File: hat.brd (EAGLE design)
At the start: 56 x 65 mm, 13 parts, among them J1 RASPBERRYPI-40-PIN-GPIO_PTH_N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

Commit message: tweaks
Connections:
- net N$1 renamed 3.3VGP10
- net N$10 renamed 5VGP18
- net N$14 renamed GP10
- net N$15 renamed GP21
- net N$18 renamed GP12
- net N$19 renamed GP18
- net N$2 renamed 3.3VGP12
- net N$3 renamed 3.3VGP18
- net N$4 renamed 3.3VGP21
- net N$7 renamed 5VGP10
- net N$8 renamed 5VGP12
- net N$9 renamed 5VGP21
- removed net N$12: C1.+, DC5VIN.1, DC5VOUT.1, INT_5V_JMPR.2, J3.2
- removed net N$13: J1.9, J2.1, J3.1
- removed net N$17: C1.-, DC5VIN.2, DC5VOUT.2, J1.6
- removed net N$5: J1.1, J2.2
- removed net N$6: INT_5V_JMPR.1, J1.2
- net 3.3V: now also J1.1, J2.2
- net 5V: now also C1.+, DC5VIN.1, DC5VOUT.1, INT_5V_JMPR.1, INT_5V_JMPR.2, J1.2, J3.2
- net GND: now also C1.-, DC5VIN.2, DC5VOUT.2, J1.6, J1.9, J2.1, J3.1
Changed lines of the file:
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@@
 <drawing>
 <settings>
-<setting alwaysvectorfont="no"/>
+<setting alwaysvectorfont="yes"/>
 <setting verticaltext="up"/>
 </settings>
@@
 <contactref element="J1" pad="34"/>
 <contactref element="J1" pad="39"/>
-<wire x1="3.81" y1="48.26" x2="6.35" y2="55.88" width="0" layer="19" extent="1-1"/>
-<wire x1="3.81" y1="43.18" x2="3.81" y2="48.26" width="0" layer="19" extent="1-1"/>
-<wire x1="6.35" y1="38.1" x2="3.81" y2="43.18" width="0" layer="19" extent="1-1"/>
-<wire x1="3.81" y1="30.48" x2="6.35" y2="38.1" width="0" layer="19" extent="1-1"/>
-<wire x1="3.81" y1="22.86" x2="3.81" y2="30.48" width="0" layer="19" extent="1-1"/>
-</signal>
-<signal name="3.3V">
-<contactref element="J1" pad="17"/>
-</signal>
-<signal name="5V">
-<contactref element="J1" pad="4"/>
-</signal>
-<signal name="N$1">
-<contactref element="J1" pad="19"/>
-<contactref element="J2" pad="6"/>
-<wire x1="13.97" y1="53.34" x2="6.35" y2="30.48" width="0" layer="19" extent="1-1"/>
-</signal>
-<signal name="N$2">
-<contactref element="J1" pad="32"/>
-<contactref element="J2" pad="5"/>
-<wire x1="13.97" y1="50.8" x2="3.81" y2="45.72" width="0" layer="19" extent="1-1"/>
-</signal>
-<signal name="N$3">
-<contactref element="J1" pad="40"/>
-<contactref element="J2" pad="3"/>
-<wire x1="13.97" y1="45.72" x2="3.81" y2="55.88" width="0" layer="19" extent="1-1"/>
-</signal>
-<signal name="N$4">
-<contactref element="J1" pad="12"/>
-<contactref element="J2" pad="4"/>
-<wire x1="13.97" y1="48.26" x2="3.81" y2="20.32" width="0" layer="19" extent="1-1"/>
-</signal>
-<signal name="N$5">
-<contactref element="J1" pad="1"/>
-<contactref element="J2" pad="2"/>
-<wire x1="6.35" y1="7.62" x2="13.97" y2="43.18" width="0" layer="19" extent="1-1"/>
-</signal>
-<signal name="N$6">
-<contactref element="J1" pad="2"/>
-<contactref element="INT_5V_JMPR" pad="1"/>
-<wire x1="11.85" y1="7.62" x2="3.81" y2="7.62" width="0" layer="19" extent="1-1"/>
-</signal>
-<signal name="N$7">
-<contactref element="J3" pad="6"/>
-<contactref element="R1" pad="1"/>
-<wire x1="24.13" y1="53.34" x2="28.36" y2="55.88" width="0" layer="19" extent="1-1"/>
-</signal>
-<signal name="N$8">
-<contactref element="J3" pad="5"/>
-<contactref element="R2" pad="1"/>
-<wire x1="24.13" y1="50.8" x2="28.36" y2="50.8" width="0" layer="19" extent="1-1"/>
-</signal>
-<signal name="N$9">
-<contactref element="J3" pad="3"/>
-<contactref element="R4" pad="1"/>
-<wire x1="24.13" y1="45.72" x2="28.36" y2="40.64" width="0" layer="19" extent="1-1"/>
-</signal>
-<signal name="N$10">
-<contactref element="J3" pad="4"/>
-<contactref element="R3" pad="1"/>
-<wire x1="24.13" y1="48.26" x2="28.36" y2="45.72" width="0" layer="19" extent="1-1"/>
-</signal>
-<signal name="N$15">
-<contactref element="R4" pad="2"/>
-<contactref element="GPIO1821" pad="2"/>
-<wire x1="52.07" y1="40.64" x2="30.06" y2="40.64" width="0" layer="19" extent="1-1"/>
-</signal>
-<signal name="N$17">
+<contactref element="J1" pad="9"/>
 <contactref element="J1" pad="6"/>
 <contactref element="DC5VIN" pad="2"/>
 <contactref element="DC5VOUT" pad="2"/>
 <contactref element="C1" pad="-"/>
-<wire x1="3.81" y1="12.7" x2="15.24" y2="16.47" width="0" layer="19" extent="1-1"/>
-<wire x1="27.94" y1="3.81" x2="3.81" y2="12.7" width="0" layer="19" extent="1-1"/>
+<contactref element="J2" pad="1"/>
+<contactref element="J3" pad="1"/>
+<wire x1="13.97" y1="40.64" x2="24.13" y2="40.64" width="0" layer="19" extent="1-1"/>
+<wire x1="6.35" y1="38.1" x2="13.97" y2="40.64" width="0" layer="19" extent="1-1"/>
+<wire x1="3.81" y1="43.18" x2="6.35" y2="38.1" width="0" layer="19" extent="1-1"/>
+<wire x1="3.81" y1="48.26" x2="3.81" y2="43.18" width="0" layer="19" extent="1-1"/>
+<wire x1="6.35" y1="55.88" x2="3.81" y2="48.26" width="0" layer="19" extent="1-1"/>
+<wire x1="3.81" y1="30.48" x2="6.35" y2="38.1" width="0" layer="19" extent="1-1"/>
+<wire x1="3.81" y1="22.86" x2="3.81" y2="30.48" width="0" layer="19" extent="1-1"/>
+<wire x1="6.35" y1="17.78" x2="3.81" y2="22.86" width="0" layer="19" extent="1-1"/>
+<wire x1="3.81" y1="12.7" x2="6.35" y2="17.78" width="0" layer="19" extent="1-1"/>
+<wire x1="15.24" y1="16.47" x2="6.35" y2="17.78" width="0" layer="19" extent="1-1"/>
+<wire x1="27.94" y1="3.81" x2="15.24" y2="16.47" width="0" layer="19" extent="1-1"/>
 <wire x1="39.37" y1="3.81" x2="27.94" y2="3.81" width="0" layer="19" extent="1-1"/>
 </signal>
-<signal name="N$12">
+<signal name="3.3V">
+<contactref element="J1" pad="17"/>
+<contactref element="J1" pad="1"/>
+<contactref element="J2" pad="2"/>
+<wire x1="6.35" y1="27.94" x2="13.97" y2="43.18" width="0" layer="19" extent="1-1"/>
+<wire x1="6.35" y1="7.62" x2="6.35" y2="27.94" width="0" layer="19" extent="1-1"/>
+</signal>
+<signal name="5V">
+<contactref element="J1" pad="4"/>
+<contactref element="J1" pad="2"/>
+<contactref element="INT_5V_JMPR" pad="1"/>
 <contactref element="DC5VIN" pad="1"/>
 <contactref element="DC5VOUT" pad="1"/>
@@
 <contactref element="J3" pad="2"/>
 <contactref element="INT_5V_JMPR" pad="2"/>
+<wire x1="15.24" y1="11.47" x2="24.13" y2="43.18" width="0" layer="19" extent="1-1"/>
 <wire x1="13.55" y1="7.62" x2="15.24" y2="11.47" width="0" layer="19" extent="1-1"/>
+<wire x1="11.85" y1="7.62" x2="13.55" y2="7.62" width="0" layer="19" extent="1-1"/>
+<wire x1="3.81" y1="7.62" x2="11.85" y2="7.62" width="0" layer="19" extent="1-1"/>
+<wire x1="3.81" y1="10.16" x2="3.81" y2="7.62" width="0" layer="19" extent="1-1"/>
 <wire x1="22.86" y1="3.81" x2="13.55" y2="7.62" width="0" layer="19" extent="1-1"/>
 <wire x1="34.29" y1="3.81" x2="22.86" y2="3.81" width="0" layer="19" extent="1-1"/>
-<wire x1="24.13" y1="43.18" x2="13.55" y2="7.62" width="0" layer="19" extent="1-1"/>
-</signal>
-<signal name="N$13">
-<contactref element="J1" pad="9"/>
-<contactref element="J2" pad="1"/>
-<contactref element="J3" pad="1"/>
-<wire x1="13.97" y1="40.64" x2="6.35" y2="17.78" width="0" layer="19" extent="1-1"/>
-<wire x1="24.13" y1="40.64" x2="13.97" y2="40.64" width="0" layer="19" extent="1-1"/>
-</signal>
-<signal name="N$14">
+</signal>
+<signal name="3.3VGP10">
+<contactref element="J1" pad="19"/>
+<contactref element="J2" pad="6"/>
+<wire x1="6.35" y1="30.48" x2="13.97" y2="53.34" width="0" layer="19" extent="1-1"/>
+</signal>
+<signal name="3.3VGP12">
+<contactref element="J1" pad="32"/>
+<contactref element="J2" pad="5"/>
+<wire x1="3.81" y1="45.72" x2="13.97" y2="50.8" width="0" layer="19" extent="1-1"/>
+</signal>
+<signal name="3.3VGP18">
+<contactref element="J1" pad="40"/>
+<contactref element="J2" pad="3"/>
+<wire x1="13.97" y1="45.72" x2="3.81" y2="55.88" width="0" layer="19" extent="1-1"/>
+</signal>
+<signal name="3.3VGP21">
+<contactref element="J1" pad="12"/>
+<contactref element="J2" pad="4"/>
+<wire x1="3.81" y1="20.32" x2="13.97" y2="48.26" width="0" layer="19" extent="1-1"/>
+</signal>
+<signal name="5VGP10">
+<contactref element="J3" pad="6"/>
+<contactref element="R1" pad="1"/>
+<wire x1="24.13" y1="53.34" x2="28.36" y2="55.88" width="0" layer="19" extent="1-1"/>
+</signal>
+<signal name="5VGP12">
+<contactref element="J3" pad="5"/>
+<contactref element="R2" pad="1"/>
+<wire x1="24.13" y1="50.8" x2="28.36" y2="50.8" width="0" layer="19" extent="1-1"/>
+</signal>
+<signal name="5VGP21">
+<contactref element="J3" pad="3"/>
+<contactref element="R4" pad="1"/>
+<wire x1="28.36" y1="40.64" x2="24.13" y2="45.72" width="0" layer="19" extent="1-1"/>
+</signal>
+<signal name="5VGP18">
+<contactref element="J3" pad="4"/>
+<contactref element="R3" pad="1"/>
+<wire x1="24.13" y1="48.26" x2="28.36" y2="45.72" width="0" layer="19" extent="1-1"/>
+</signal>
+<signal name="GP21">
+<contactref element="R4" pad="2"/>
+<contactref element="GPIO1821" pad="2"/>
+<wire x1="30.06" y1="40.64" x2="52.07" y2="40.64" width="0" layer="19" extent="1-1"/>
+</signal>
+<signal name="GP10">
 <contactref element="R1" pad="2"/>
 <contactref element="GPIO1012" pad="1"/>
-<wire x1="52.07" y1="55.88" x2="30.06" y2="55.88" width="0" layer="19" extent="1-1"/>
-</signal>
-<signal name="N$18">
+<wire x1="30.06" y1="55.88" x2="52.07" y2="55.88" width="0" layer="19" extent="1-1"/>
+</signal>
+<signal name="GP12">
 <contactref element="R2" pad="2"/>
 <contactref element="GPIO1012" pad="2"/>
-<wire x1="52.07" y1="50.8" x2="30.06" y2="50.8" width="0" layer="19" extent="1-1"/>
-</signal>
-<signal name="N$19">
+<wire x1="30.06" y1="50.8" x2="52.07" y2="50.8" width="0" layer="19" extent="1-1"/>
+</signal>
+<signal name="GP18">
 <contactref element="R3" pad="2"/>
 <contactref element="GPIO1821" pad="1"/>
-<wire x1="52.07" y1="45.72" x2="30.06" y2="45.72" width="0" layer="19" extent="1-1"/>
+<wire x1="30.06" y1="45.72" x2="52.07" y2="45.72" width="0" layer="19" extent="1-1"/>
 </signal>
 </signals>

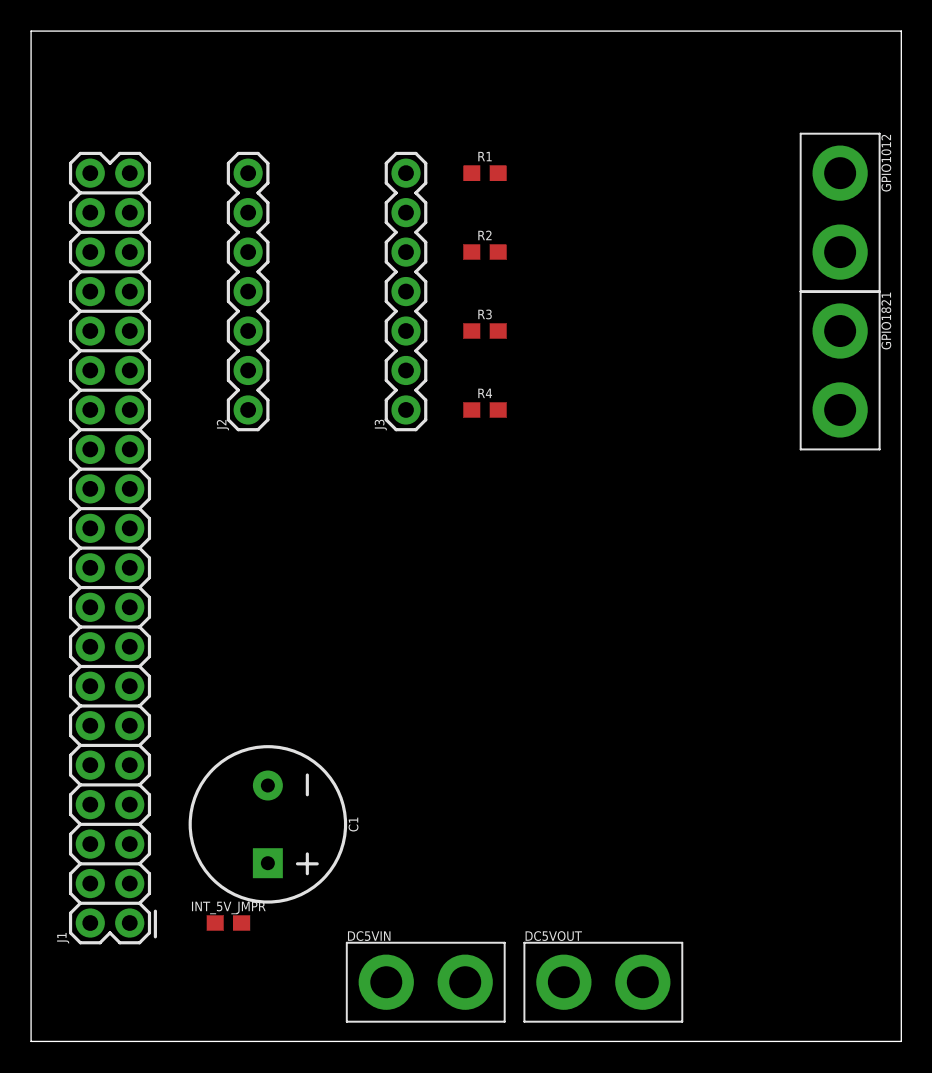
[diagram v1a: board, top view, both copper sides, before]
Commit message: shrunk board, double sided
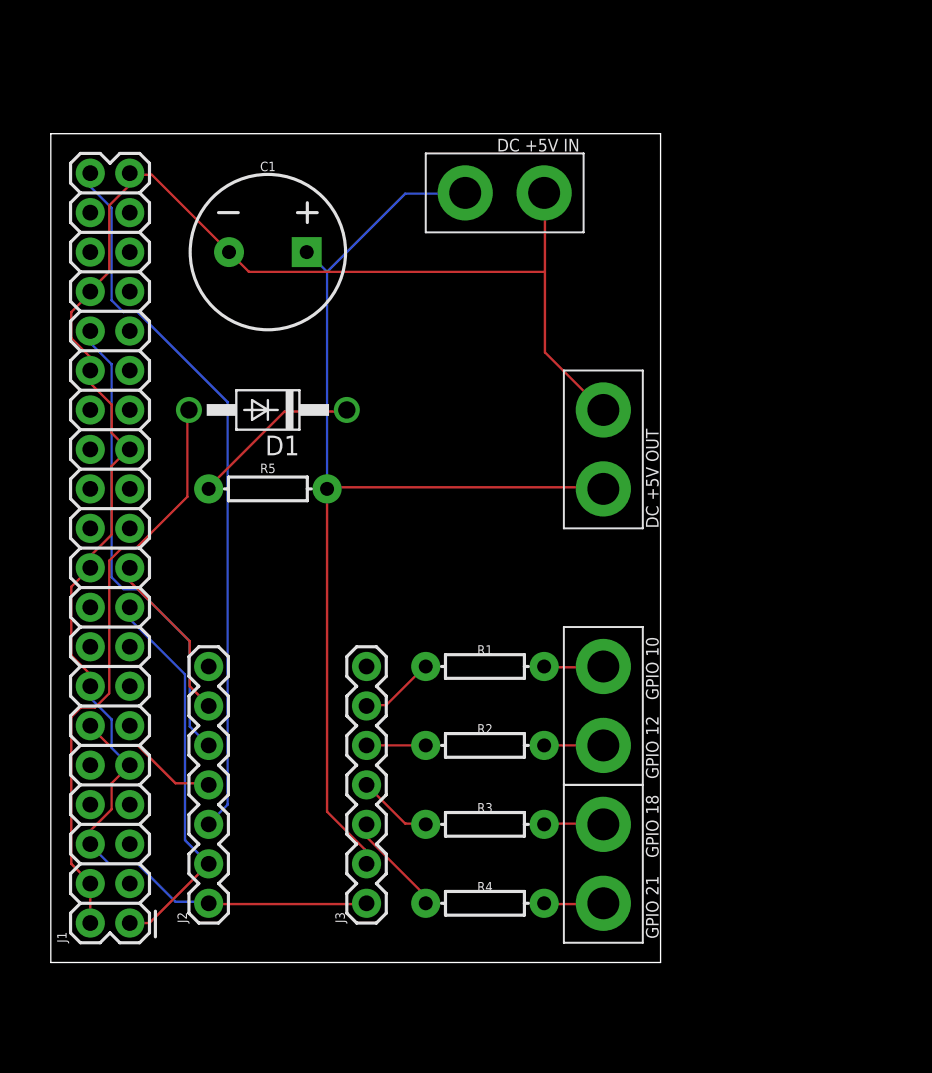
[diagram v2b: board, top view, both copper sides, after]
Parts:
- removed INT_5V_JMPR: 0, SparkFun-Resistors:0603
- added D1: 1N4004, diode:DO41-10
- added R5: (no value), SparkFun-Resistors:AXIAL-0.3
- R1, R2, R3, R4: value 470 -> (none); device SparkFun-Resistors:0603 -> SparkFun-Resistors:AXIAL-0.3
- moved DC5VIN 51.1 mm to (30.5, 54.6)
- moved C1 36.8 mm to (15.2, 50.8), turned to 0 degrees
- moved GPIO1012 35.2 mm to (36.8, 21.6)
- moved GPIO1821 35.2 mm to (36.8, 11.4)
- moved DC5VOUT 34.3 mm to (36.8, 38.1), turned to 90 degrees
- moved J2 31.9 mm to (11.4, 8.89)
- moved J3 31.9 mm to (21.6, 8.89)
- moved R1 31.8 mm to (29.2, 24.1)
- moved R3 31.8 mm to (29.2, 14.0)
- moved R4 31.8 mm to (29.2, 8.89)
- moved R2 31.7 mm to (29.2, 19.1)
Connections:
- new net N$5: D1.C, R5.P$1
- new net N$6: C1.+, DC5VIN.1, DC5VOUT.1, J3.2, R5.P$2
- net 3.3VGP18: now also J1.12, J2.4; no longer J1.40, J2.3
- net 3.3VGP21: now also J1.40, J2.3; no longer J1.12, J2.4
- net 5V: now also D1.A; no longer C1.+, DC5VIN.1, DC5VOUT.1, INT_5V_JMPR.1, INT_5V_JMPR.2, J3.2
- net 5VGP10: now also R1.P$1; no longer R1.1
- net 5VGP12: now also R2.P$1; no longer R2.1
- net 5VGP18: now also R3.P$1; no longer R3.1
- net 5VGP21: now also R4.P$1; no longer R4.1
- net GP10: now also R1.P$2; no longer R1.2
- net GP12: now also R2.P$2; no longer R2.2
- net GP18: now also R3.P$2; no longer R3.2
- net GP21: now also R4.P$2; no longer R4.2
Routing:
- net GND: track 0.00 -> 115.0 mm
- net N$6: track 0.00 -> 70.0 mm
- net 3.3VGP21: track 0.00 -> 46.6 mm
- net 5V: track 0.00 -> 37.7 mm
- net 3.3VGP12: track 0.00 -> 30.4 mm
- net 3.3V: track 0.00 -> 25.3 mm
- net N$5: track 0.00 -> 11.1 mm
- net 3.3VGP10: track 0.00 -> 11.0 mm
- net 3.3VGP18: track 0.00 -> 9.29 mm
- net 5VGP21: track 0.00 -> 6.65 mm
- net 5VGP18: track 0.00 -> 4.85 mm
- net 5VGP10: track 0.00 -> 4.85 mm
- net GP21: track 0.00 -> 3.84 mm
- net GP18: track 0.00 -> 3.84 mm
- net GP10: track 0.00 -> 3.84 mm
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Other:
- board size 56 x 65 mm -> 39.2 x 53.3 mm
- board text added: "GPIO 10"
- board text added: "GPIO 12"
- board text added: "GPIO 18"
- board text added: "GPIO 21"
